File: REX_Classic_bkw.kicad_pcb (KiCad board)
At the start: 2 copper layers, 16 x 38 mm, 13 parts, among them J1 Molex_DIP28_edge_contacts, J2 JTAG, J3 PRG, U1 XCR3064XL-10VQ44, U2 29F800, U3 LP2980-3.3

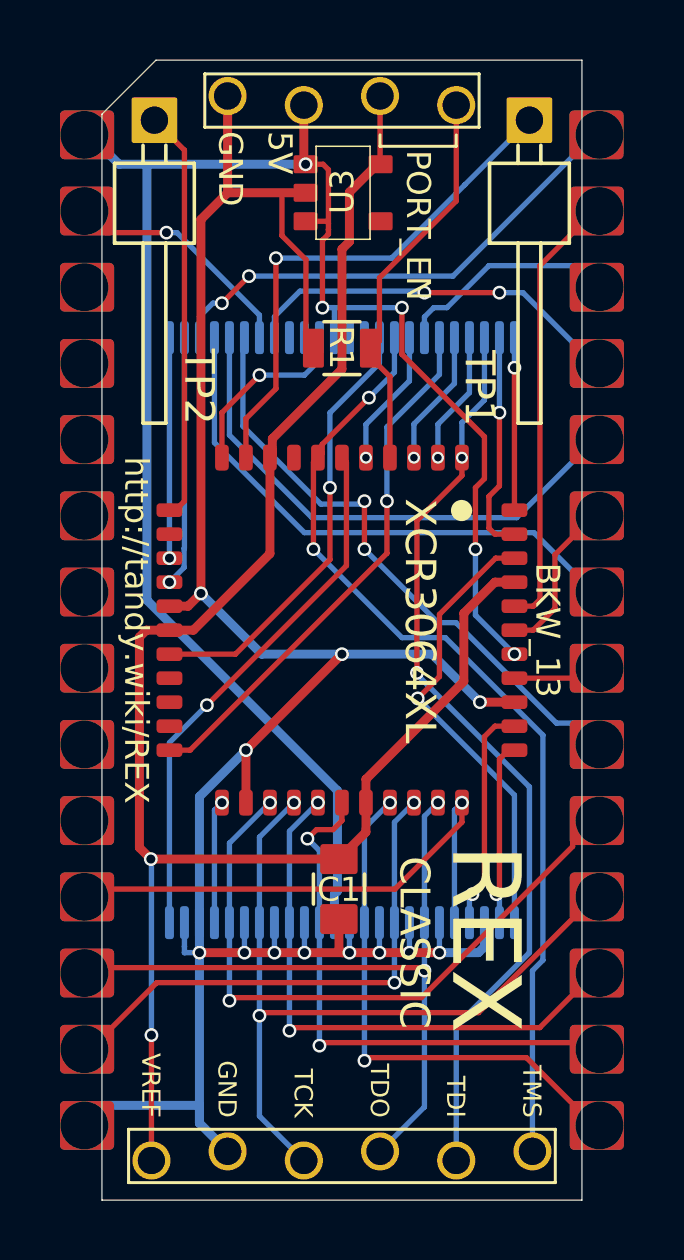
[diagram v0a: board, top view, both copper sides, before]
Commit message: Less expensive manufacturing tolerances. Rename to REX Classic.
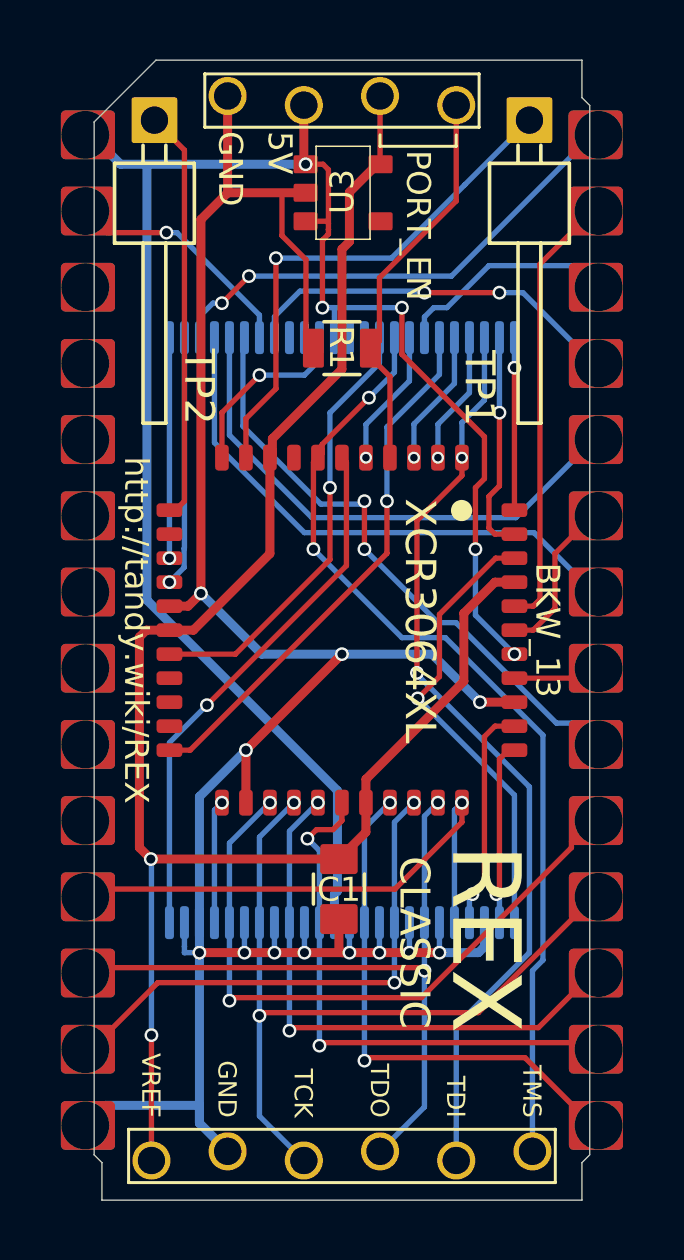
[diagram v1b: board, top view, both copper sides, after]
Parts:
- J1: footprint 000_LOCAL:pcb2molex8878 -> 000_LOCAL:pcb2molex8878_contacts
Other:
- board size 16 x 38 mm -> 16.5 x 38 mm
- net class Default: via_dia 0.4 -> 0.46; via_drill 0.25 -> 0.3
- rule via_min_drill: 0.25 -> 0.3
- rule via_min_size: 0.4 -> 0.46

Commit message: min drill 0.3mm for PCBWAY, replace GND traces with zone fill
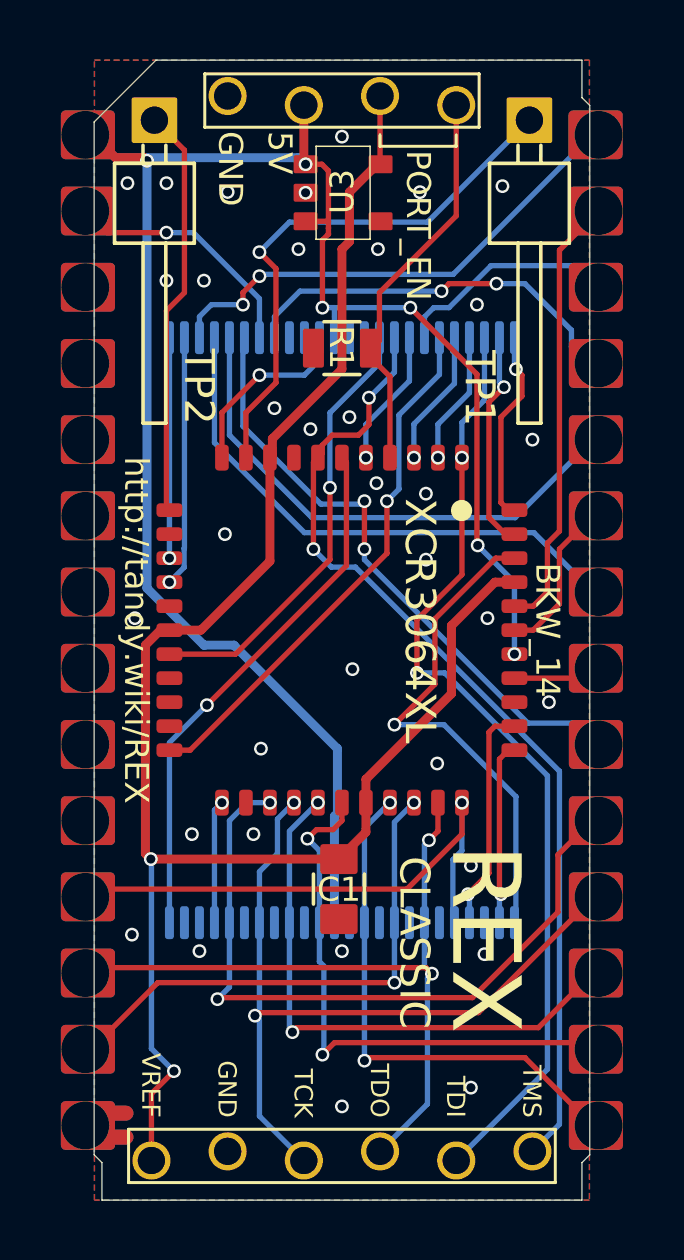
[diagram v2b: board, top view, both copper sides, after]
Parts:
- removed NT2: Net-Tie_2, 000_LOCAL:Net_Tie_2_0.18mm
- removed carrier?: pcb2molex8878_chamfer, 000_LOCAL:pcb2molex8878_chamfer
- J1: value Molex_DIP28_edge_contacts -> TRS-80_Model_100_Option_ROM; footprint 000_LOCAL:pcb2molex8878_contacts -> 000_LOCAL:pcb2molex8878
- moved NT1 0.15 mm to (146.8, 85.9), turned to 90 degrees
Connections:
- net /D1 renamed /D1_TDO
- net /D6 renamed /D6_TCK
- net /LVA19 renamed /LVA19_TMS
- net /LVA4 renamed /LVA4_TDI
- net /RY_BY renamed /RY~BY
- net /~CE renamed /~CE_MEM
- net /~CS renamed /~CS_BUS
- net /~OE renamed /~OE_MEM
- net /~RD renamed /~OE_BUS
- J1 pad 1: /+5 -> +5V
- J3 pad 2: /+5 -> +5V
- NT1 pad 1: /+5 -> /~RESET
- NT1 pad 2: /~RESET -> +5V
- U2 pad 37: /+5 -> +5V
- U2 pad 47: /~BYTE -> GND
- U3 pad 1: /+5 -> +5V
- U3 pad 3: /+5 -> +5V
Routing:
- net GND: track 83.8 -> 6.95 mm, vias 12 -> 35
- net +5V: track 0.00 -> 44.3 mm, vias 0 -> 2
- net /+5: track 41.1 -> 0.00 mm, vias 1 -> 0
- net /D7: track 22.1 -> 24.0 mm
- net /LVA1: track 15.2 -> 16.9 mm
- net /LVA4_TDI: track 30.9 -> 32.0 mm
- net /TP1: track 17.4 -> 18.3 mm
- net /~BYTE: track 0.80 -> 0.00 mm
- net /LVA2: track 5.75 -> 6.45 mm
- net /LVA19_TMS: track 32.4 -> 33.0 mm
- net /A9: track 12.9 -> 13.4 mm
- added copper zone on B.Cu, net GND
- added copper zone on F.Cu, net GND
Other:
- board text added: "BKW_14"
- board text removed: "BKW_13"

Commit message: rename pcb2molex8878 to Molex78805_PCB
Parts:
- J1: footprint 000_LOCAL:pcb2molex8878 -> 000_LOCAL:Molex78805_PCB

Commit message: clearances
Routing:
- net /~OE_MEM: track 7.59 -> 9.95 mm
- net /LVA15: track 8.36 -> 9.26 mm
- net /TP1: track 18.3 -> 17.5 mm
- net /LVA2: track 6.45 -> 5.79 mm
- net +5V: track 44.3 -> 43.7 mm
- net /A8: track 7.53 -> 6.89 mm
- net /~RESET: track 19.5 -> 18.8 mm
- net /LVA16: track 7.35 -> 7.96 mm
- net /A9: track 13.4 -> 14.0 mm
- net GND: vias 35 -> 9
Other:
- board text added: "BKW_16"
- board text removed: "BKW_14"

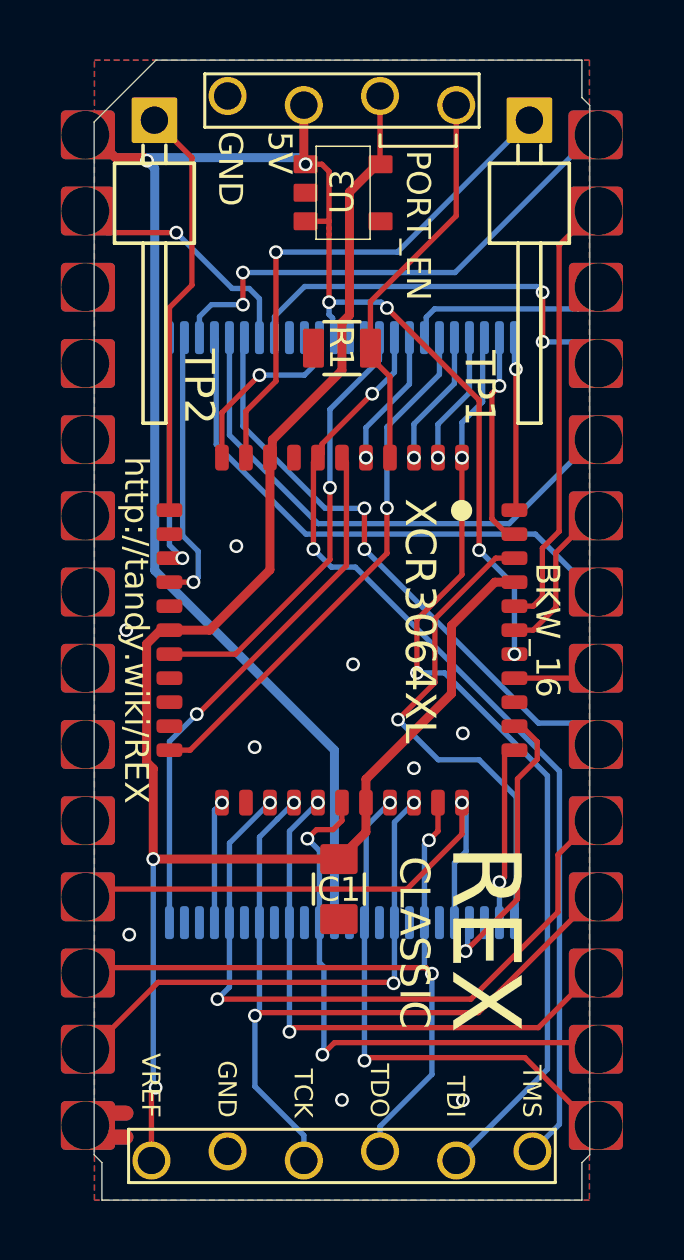
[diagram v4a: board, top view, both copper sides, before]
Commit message: upgrade board outline and carrier to v004
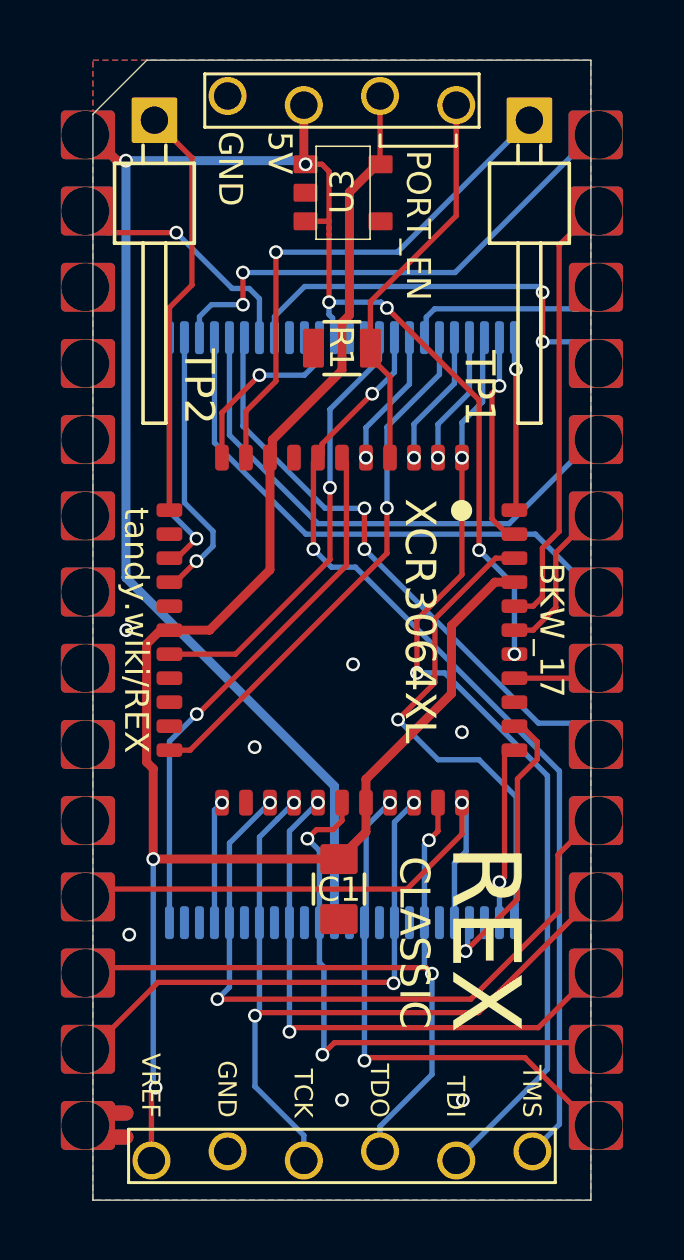
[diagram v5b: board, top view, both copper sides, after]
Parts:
- J1: footprint 000_LOCAL:Molex78805_PCB -> 000_LOCAL:Molex78802_PCB_28
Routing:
- net GND: vias 9 -> 7
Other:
- board size 16.5 x 38 mm -> 16.6 x 38 mm
- board text added: "BKW_17"
- board text added: "tandy.wiki/REX"
- board text removed: "BKW_16"
- board text removed: "http://tandy.wiki/REX"

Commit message: remove pointless busses from sch, minor silkscreen tweaks
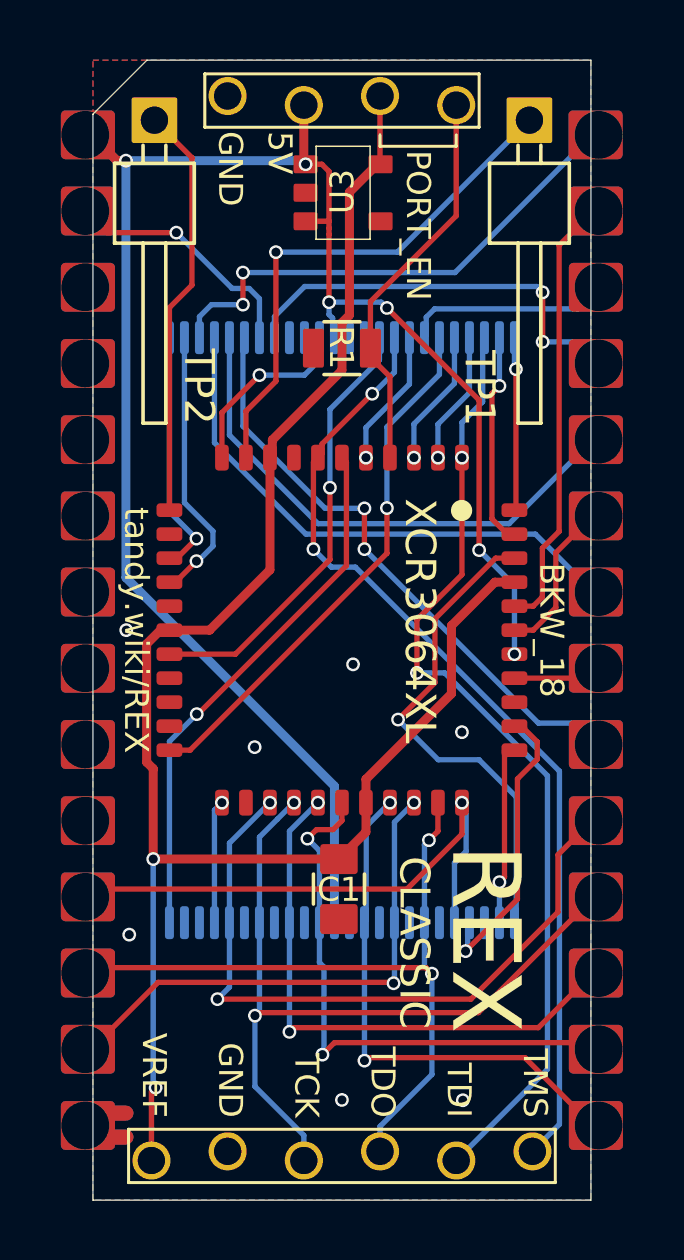
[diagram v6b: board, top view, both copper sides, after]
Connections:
- net /TP1 renamed Net-(TP1-Pad1)
- net /TP2 renamed Net-(TP2-Pad1)
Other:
- board text added: "BKW_18"
- board text added: "shpws.me/SGGB"
- board text removed: "BKW_17"

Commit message: clearance around some traces & vias
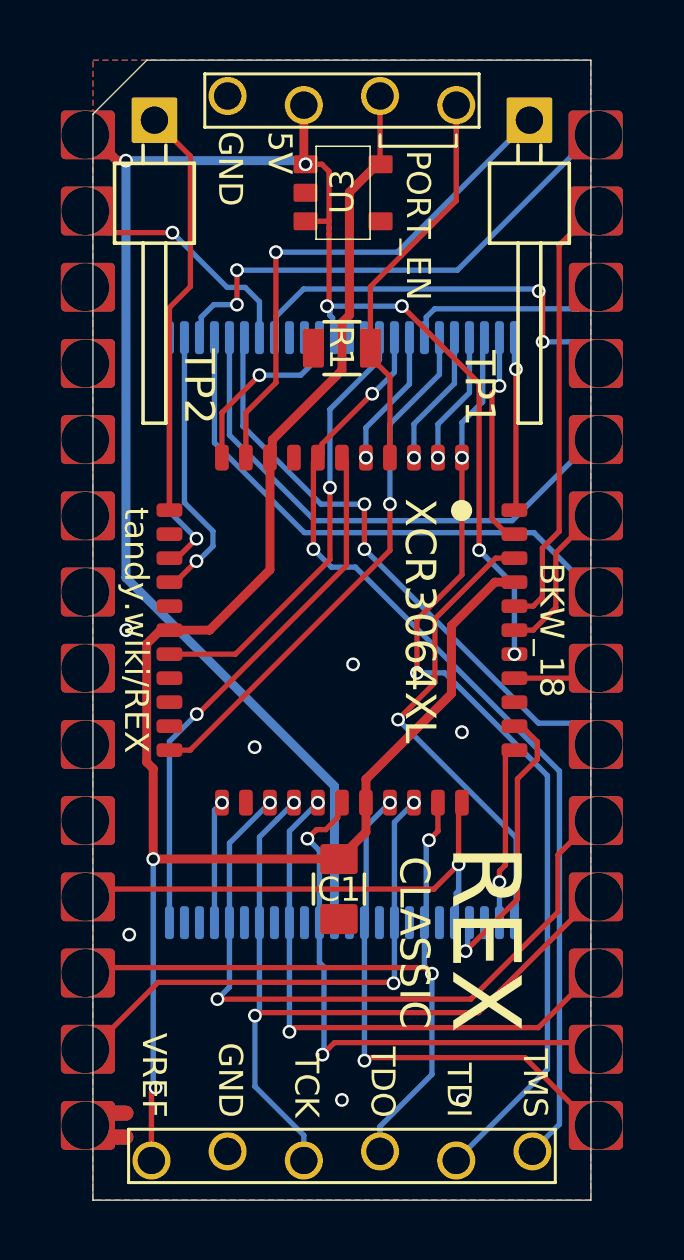
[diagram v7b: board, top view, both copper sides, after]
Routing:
- net /D0: track 18.7 -> 17.0 mm
- net /LVA1: track 16.6 -> 15.8 mm

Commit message: clearances, remove pointless busses in schematic
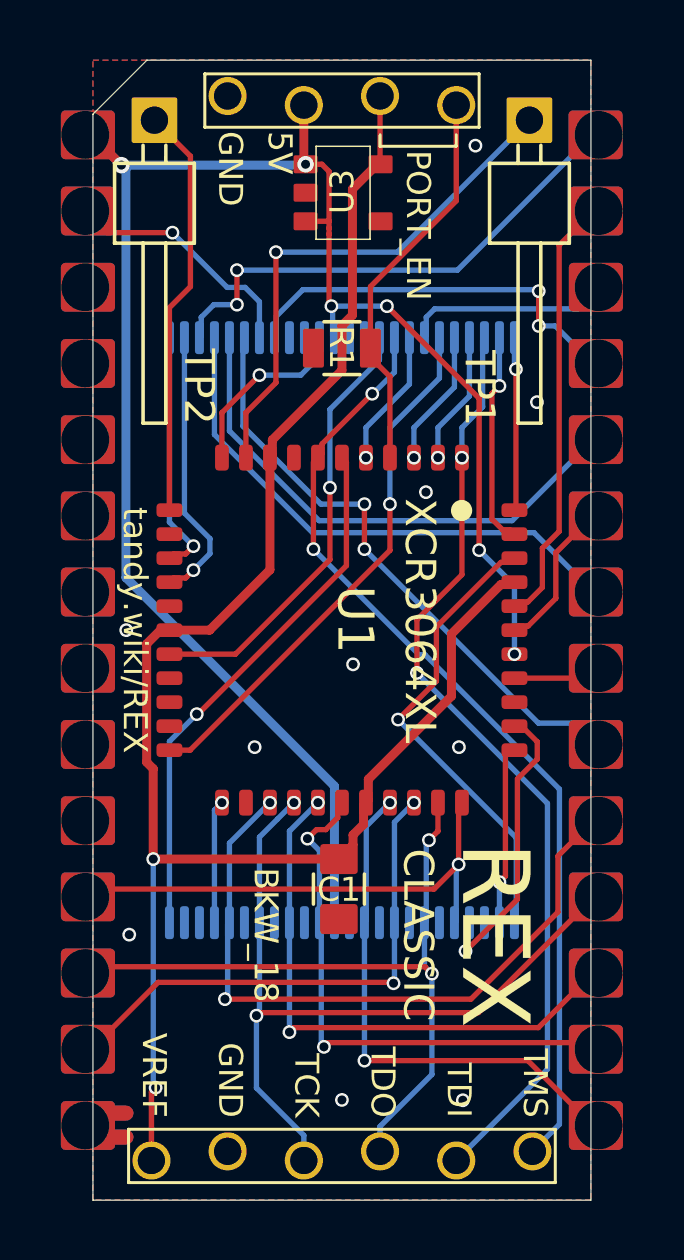
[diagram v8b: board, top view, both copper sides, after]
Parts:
- U1: value XCR3064XL-10VQ44 -> XCR3064XL-VQ44; footprint 000_LOCAL:QFP44 -> 000_LOCAL:VQFP44
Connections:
- U1 pad 34: /~CE_MEM -> (no net)
- U2 pad 26: /~CE_MEM -> (no net)
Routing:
- net /~CE_MEM: track 6.13 -> 0.00 mm, vias 1 -> 0
- net (no net): track 0.00 -> 6.13 mm, vias 0 -> 1
- net /LVA4_TDI: track 32.0 -> 31.4 mm
- net GND: vias 7 -> 10
